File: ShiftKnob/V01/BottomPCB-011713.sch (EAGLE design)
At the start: 34 parts, among them IC2 7805DT, Q1 16MHz, Q2 MOSFET-NCHANNELSMD, Q3 MOSFET-NCHANNELSMD, U1 ATMEGA328

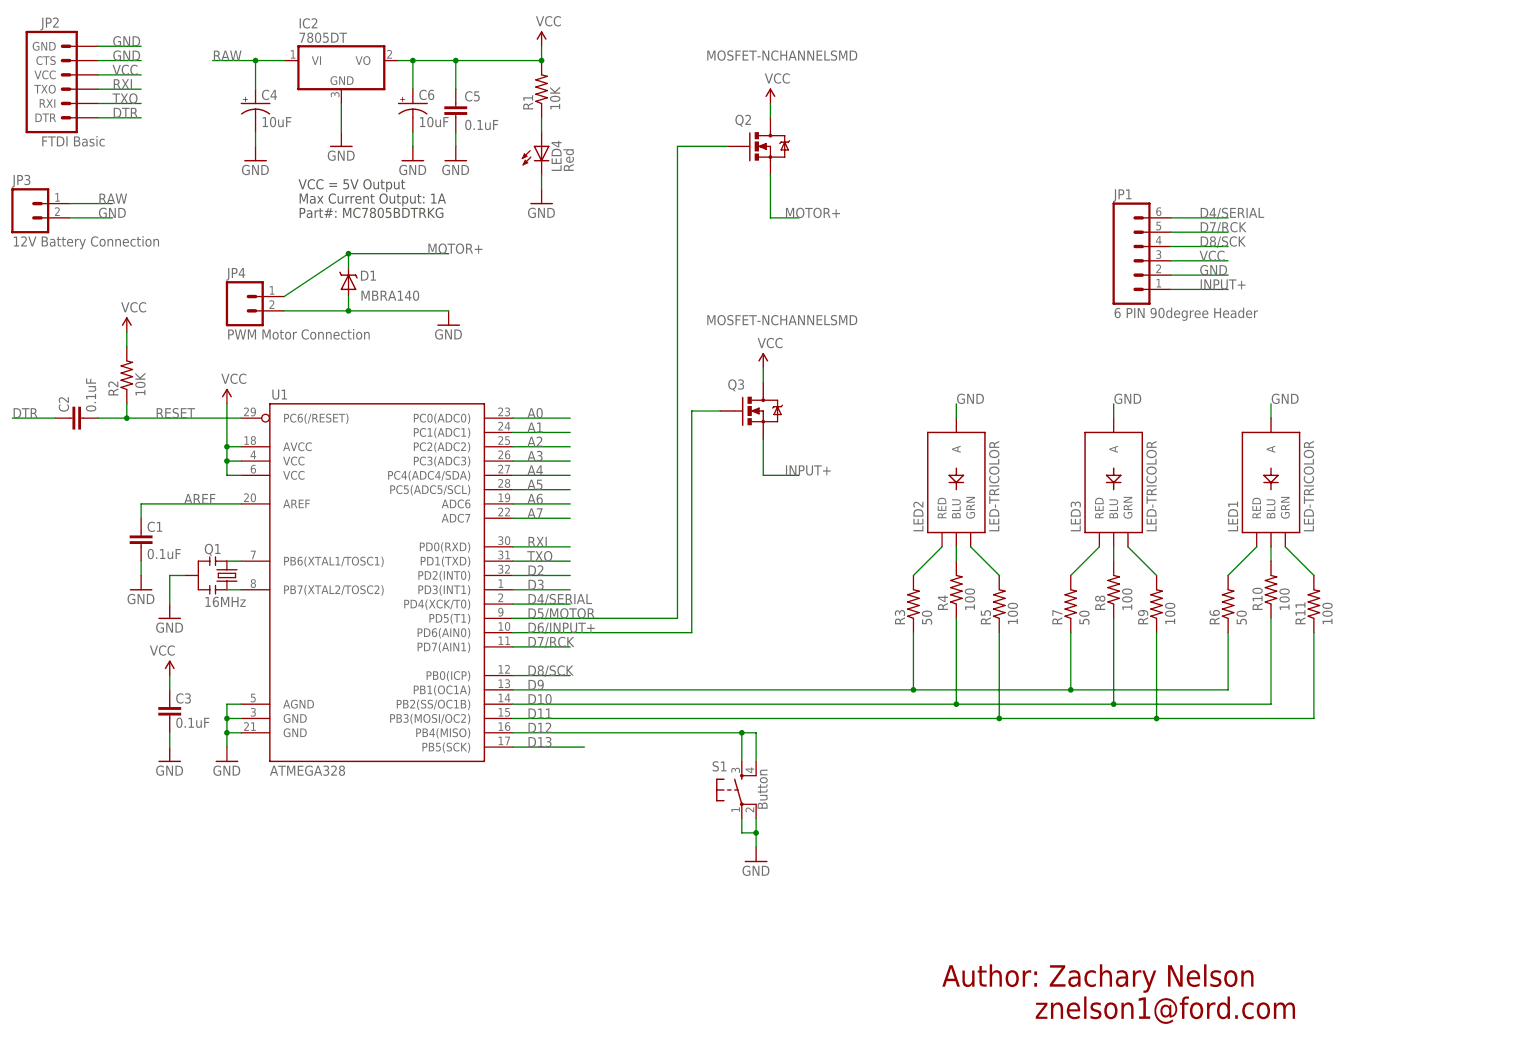
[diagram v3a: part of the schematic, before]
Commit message: switch pins on battery connector and motor connector to match footprint
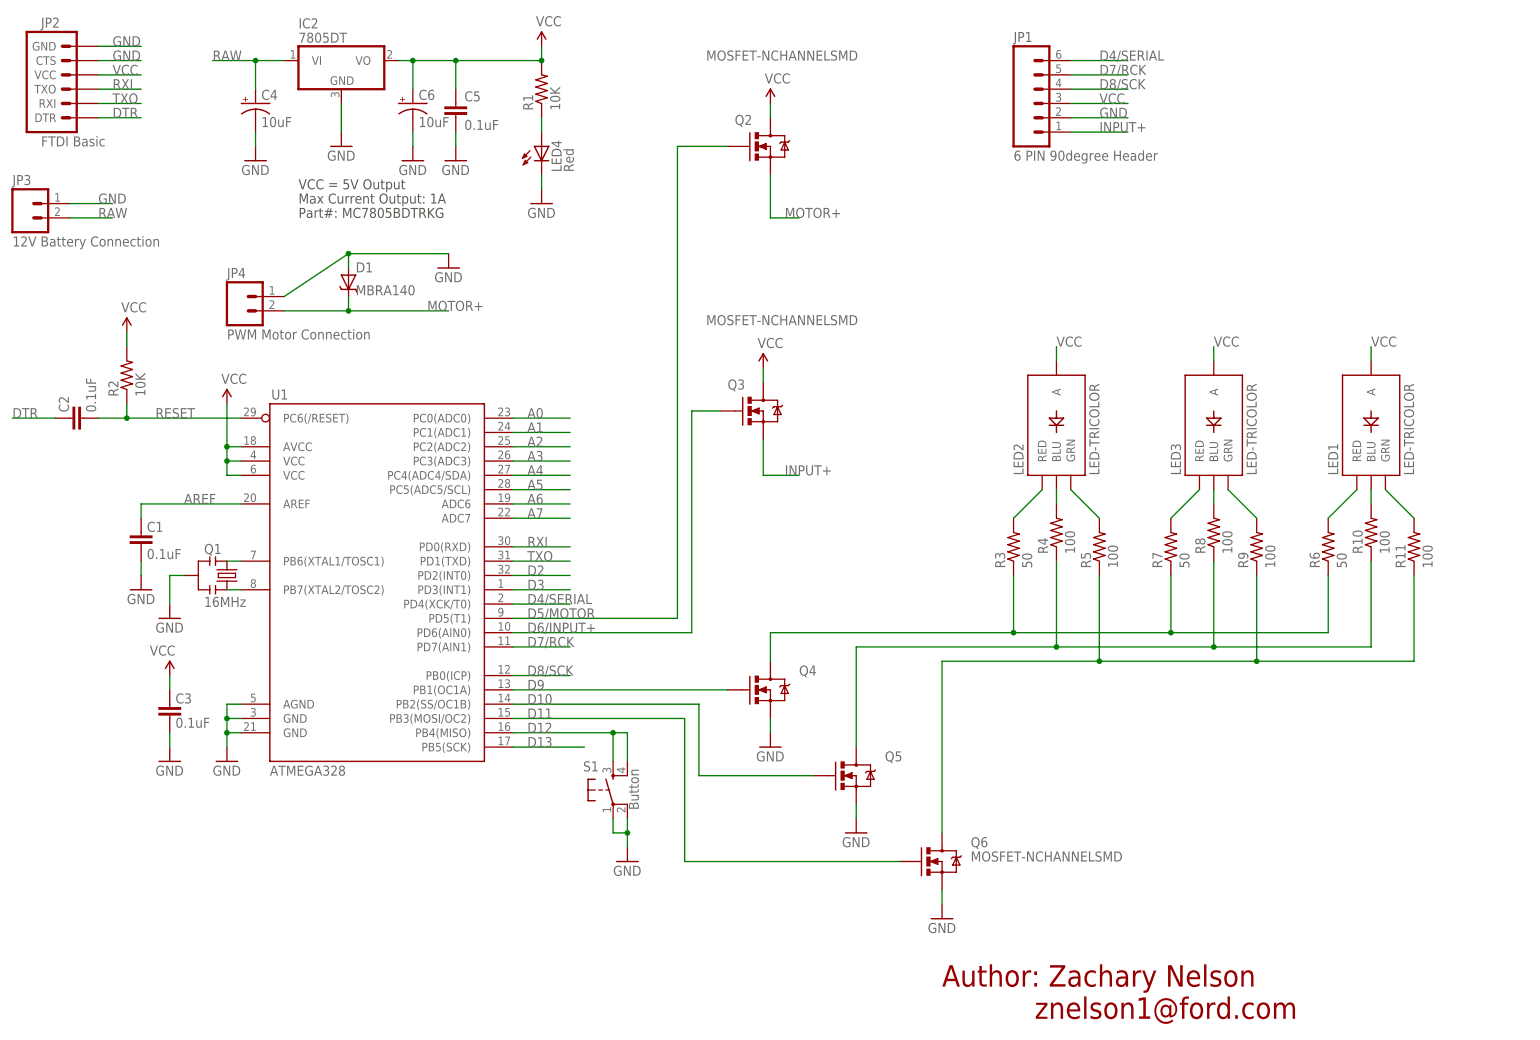
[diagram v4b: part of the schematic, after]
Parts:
- added Q4, Q5, Q6: MOSFET-NCHANNELSMD, SparkFun-DiscreteSemi:MOSFET-NCHANNELSMD
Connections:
- new net N$11: Q4.G, U1.PB1(OC1A)
- new net N$12: Q5.G, U1.PB2(SS/OC1B)
- new net N$15: Q6.G, U1.PB3(MOSI/OC2)
- net D10: now also Q5.D; no longer U1.PB2(SS/OC1B)
- net D11: now also Q6.D; no longer U1.PB3(MOSI/OC2)
- net D9: now also Q4.D; no longer U1.PB1(OC1A)
- net GND: now also JP3.2, JP4.2, Q4.S, Q5.S, Q6.S; no longer JP3.1, JP4.1, LED1.A, LED2.A, LED3.A
- net MOTOR+: now also JP4.1; no longer JP4.2
- net RAW: now also JP3.1; no longer JP3.2
- net VCC: now also LED1.A, LED2.A, LED3.A
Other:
- moved on the sheet: D1, JP1, LED1, LED2, LED3, R10, R11, R3, R4, R5, R6, R7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

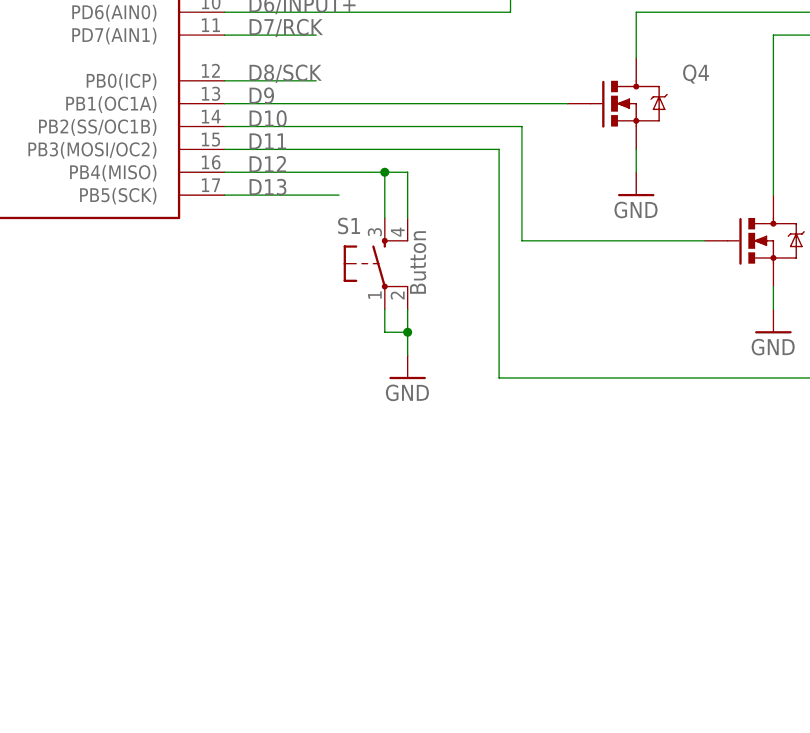
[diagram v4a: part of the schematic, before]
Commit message: add pullup resistor to button. adding traces to board.
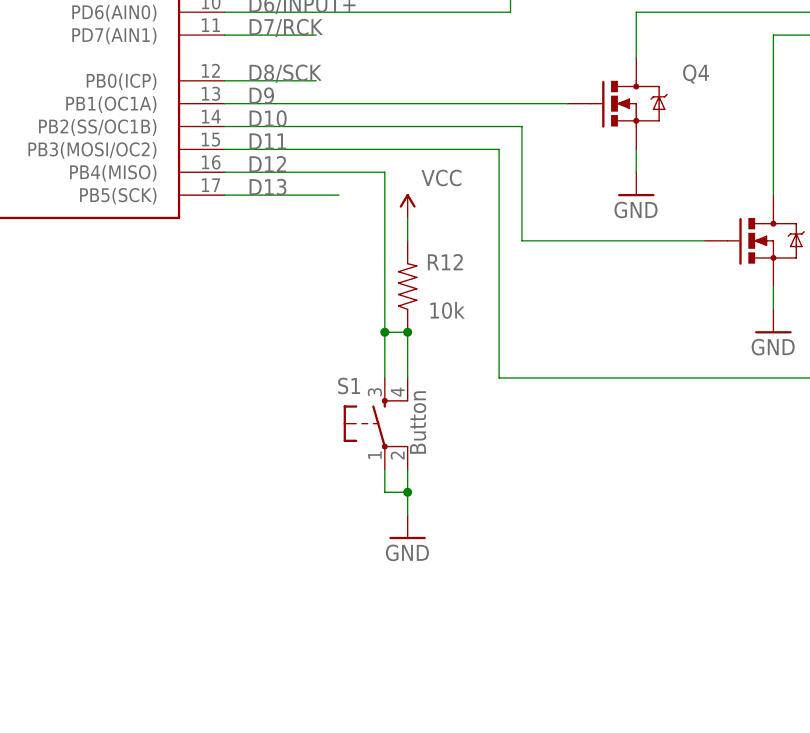
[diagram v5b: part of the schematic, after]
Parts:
- added R12: 10k, SparkFun-Passives:RESISTOR0402-RES
- JP1: device SparkFun-Connectors:M06POGOPIN_HOLES_ONLY -> SparkFun-Connectors:M06SIP
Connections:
- new net 3.3V: R12.2
- net D12: now also R12.1
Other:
- moved on the sheet: S1
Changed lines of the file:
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@@
 <setting verticaltext="up"/>
 </settings>
-<grid distance="0.05" unitdist="inch" unit="inch" style="lines" multiple="1" display="no" altdistance="0.01" altunitdist="inch" altunit="inch"/>
+<grid distance="0.1" unitdist="inch" unit="inch" style="lines" multiple="1" display="no" altdistance="0.01" altunitdist="inch" altunit="inch"/>
 <layers>
 <layer number="1" name="Top" color="4" fill="1" visible="no" active="no"/>
@@
 <parts>
 <part name="FRAME1" library="frames" deviceset="FRAME_A_L" device=""/>
-<part name="JP1" library="SparkFun-Connectors" deviceset="M06" device="POGOPIN_HOLES_ONLY" value="6 PIN 90degree Header"/>
+<part name="JP1" library="SparkFun-Connectors" deviceset="M06" device="SIP" value="6 PIN 90degree Header"/>
 <part name="FRAME2" library="SparkFun" deviceset="FRAME-LETTER" device=""/>
 <part name="R2" library="SparkFun" deviceset="RESISTOR" device="0402-RES" value="10K"/>
@@
 <part name="GND13" library="SparkFun" deviceset="GND" device=""/>
 <part name="GND14" library="SparkFun" deviceset="GND" device=""/>
+<part name="P+2" library="SparkFun" deviceset="3.3V" device="" value="VCC"/>
+<part name="R12" library="SparkFun-Passives" deviceset="RESISTOR" device="0402-RES" value="10k"/>
 </parts>
 <sheets>
@@
 <instance part="FRAME2" gate="G$2" x="447.04" y="17.78"/>
 <instance part="R2" gate="G$1" x="30.48" y="139.7" rot="R90"/>
-<instance part="S1" gate="S" x="116.84" y="66.04" smashed="yes" rot="R90">
-<attribute name="NAME" x="111.506" y="69.342" size="1.778" layer="95"/>
-<attribute name="VALUE" x="121.412" y="62.484" size="1.778" layer="96" rot="R90"/>
-</instance>
-<instance part="GND3" gate="1" x="119.38" y="53.34"/>
+<instance part="S1" gate="S" x="116.84" y="48.26" smashed="yes" rot="R90">
+<attribute name="NAME" x="111.506" y="51.562" size="1.778" layer="95"/>
+<attribute name="VALUE" x="121.412" y="44.704" size="1.778" layer="96" rot="R90"/>
+</instance>
+<instance part="GND3" gate="1" x="119.38" y="35.56"/>
 <instance part="C3" gate="G$1" x="38.1" y="81.28" smashed="yes" rot="R180">
 <attribute name="NAME" x="39.116" y="81.407" size="1.778" layer="95"/>
@@
 <instance part="GND13" gate="1" x="160.02" y="58.42"/>
 <instance part="GND14" gate="1" x="175.26" y="43.18"/>
+<instance part="P+2" gate="G$1" x="119.38" y="71.12" smashed="yes">
+<attribute name="VALUE" x="120.904" y="74.676" size="1.778" layer="96"/>
+</instance>
+<instance part="R12" gate="G$1" x="119.38" y="63.5" smashed="yes" rot="R90">
+<attribute name="NAME" x="125.73" y="67.0814" size="1.778" layer="95" rot="R180"/>
+<attribute name="VALUE" x="125.73" y="61.722" size="1.778" layer="96" rot="R180"/>
+</instance>
 </instances>
 <busses>
@@
 </segment>
 <segment>
-<wire x1="116.84" y1="60.96" x2="116.84" y2="58.42" width="0.1524" layer="91"/>
-<wire x1="116.84" y1="58.42" x2="119.38" y2="58.42" width="0.1524" layer="91"/>
-<wire x1="119.38" y1="58.42" x2="119.38" y2="60.96" width="0.1524" layer="91"/>
-<wire x1="119.38" y1="58.42" x2="119.38" y2="55.88" width="0.1524" layer="91"/>
-<junction x="119.38" y="58.42"/>
+<wire x1="116.84" y1="43.18" x2="116.84" y2="40.64" width="0.1524" layer="91"/>
+<wire x1="116.84" y1="40.64" x2="119.38" y2="40.64" width="0.1524" layer="91"/>
+<wire x1="119.38" y1="40.64" x2="119.38" y2="43.18" width="0.1524" layer="91"/>
+<wire x1="119.38" y1="40.64" x2="119.38" y2="38.1" width="0.1524" layer="91"/>
+<junction x="119.38" y="40.64"/>
 <pinref part="S1" gate="S" pin="1"/>
 <pinref part="S1" gate="S" pin="2"/>
@@
 <pinref part="S1" gate="S" pin="3"/>
 <wire x1="99.06" y1="76.2" x2="116.84" y2="76.2" width="0.1524" layer="91"/>
-<wire x1="116.84" y1="76.2" x2="116.84" y2="71.12" width="0.1524" layer="91"/>
+<wire x1="116.84" y1="76.2" x2="116.84" y2="58.42" width="0.1524" layer="91"/>
+<wire x1="116.84" y1="58.42" x2="116.84" y2="53.34" width="0.1524" layer="91"/>
 <pinref part="S1" gate="S" pin="4"/>
-<wire x1="116.84" y1="76.2" x2="119.38" y2="76.2" width="0.1524" layer="91"/>
-<wire x1="119.38" y1="76.2" x2="119.38" y2="71.12" width="0.1524" layer="91"/>
-<junction x="116.84" y="76.2"/>
+<wire x1="116.84" y1="58.42" x2="119.38" y2="58.42" width="0.1524" layer="91"/>
+<wire x1="119.38" y1="58.42" x2="119.38" y2="53.34" width="0.1524" layer="91"/>
+<junction x="116.84" y="58.42"/>
+<pinref part="R12" gate="G$1" pin="1"/>
+<junction x="119.38" y="58.42"/>
 </segment>
 </net>
@@
 </segment>
 </net>
+<net name="3.3V" class="0">
+<segment>
+<pinref part="R12" gate="G$1" pin="2"/>
+<pinref part="P+2" gate="G$1" pin="3.3V"/>
+<wire x1="119.38" y1="71.12" x2="119.38" y2="68.58" width="0.1524" layer="91"/>
+</segment>
+</net>

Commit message: add more traces to brd layout. not yet finished.
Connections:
- removed net 3.3V: R12.2
- net VCC: now also R12.2
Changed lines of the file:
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@@
 <label x="251.46" y="144.78" size="1.778" layer="95"/>
+</segment>
+<segment>
+<pinref part="R12" gate="G$1" pin="2"/>
+<pinref part="P+2" gate="G$1" pin="3.3V"/>
+<wire x1="119.38" y1="71.12" x2="119.38" y2="68.58" width="0.1524" layer="91"/>
 </segment>
 </net>
@@
 </segment>
 </net>
-<net name="3.3V" class="0">
-<segment>
-<pinref part="R12" gate="G$1" pin="2"/>
-<pinref part="P+2" gate="G$1" pin="3.3V"/>
-<wire x1="119.38" y1="71.12" x2="119.38" y2="68.58" width="0.1524" layer="91"/>
-</segment>
-</net>
